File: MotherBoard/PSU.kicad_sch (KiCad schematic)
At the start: 51 parts, among them U401 LMR51430, U402 LMR51430

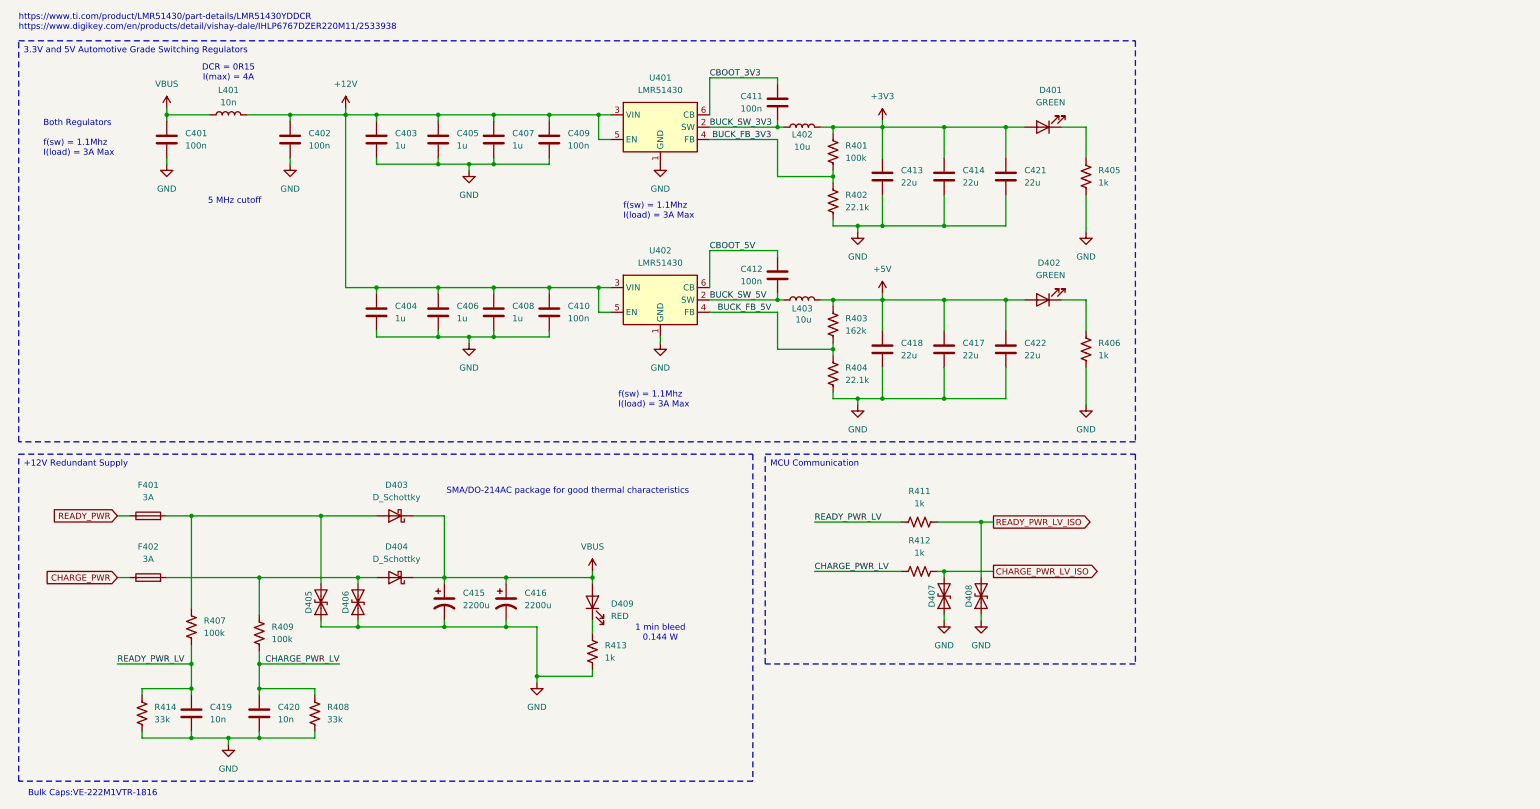
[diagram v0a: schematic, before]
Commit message: Redesigned EMI filters for switching regulators to meet CISPR 25 Class 5 EMI constraint + substituted BOM #s for JLC basic parts
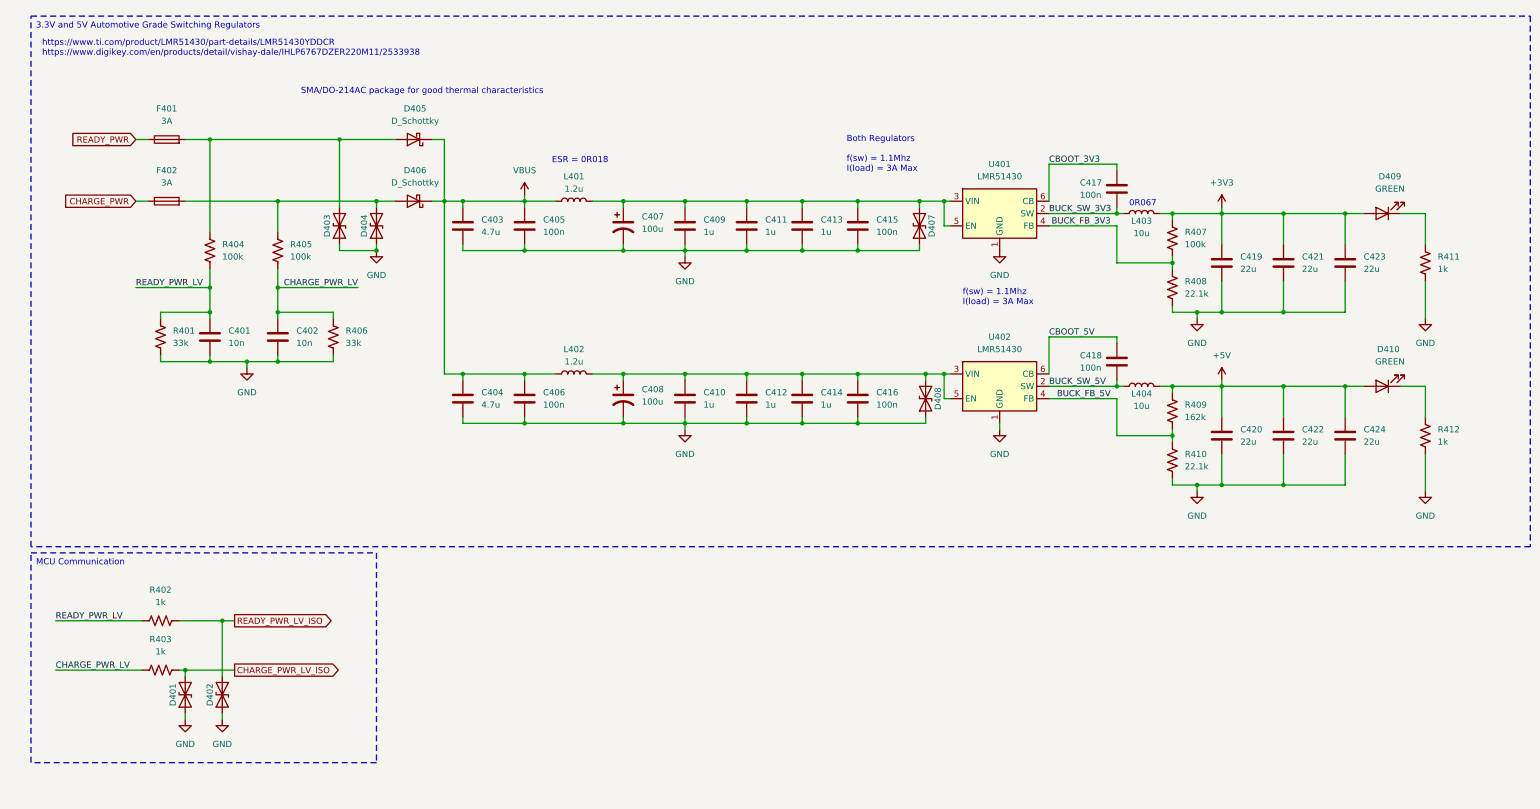
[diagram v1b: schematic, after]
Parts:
- removed C401, C402: 100n, Capacitor_SMD:C_0402_1005Metric, symbol Device:C
- removed C415, C416: 2200u, Capacitor_SMD:CP_Elec_18x17.5, symbol Device:C_Polarized_US
- removed D409: RED, LED_SMD:LED_0603_1608Metric, symbol Device:LED
- removed L403: 10u, symbol Device:L
- removed R413: 1k, Resistor_SMD:R_2512_6332Metric, symbol Device:R_US
- added C403, C404: 4.7u, Capacitor_SMD:C_1206_3216Metric, symbol Device:C
- added C405, C406: 100n, Capacitor_SMD:C_0402_1005Metric, symbol Device:C
- added C407, C408: 100u, Capacitor_SMD:CP_Elec_6.3x5.8, symbol Device:C_Polarized_US
- added D407, D408: D_TVS, Diode_SMD:D_SOD-323, symbol Device:D_TVS
- added L402: 1.2u, symbol Device:L
- added L404: 10u, Inductor_SMD:L_Sunlord_MWSA0603S, symbol Device:L
- C415: renamed from C409; footprint Capacitor_SMD:C_0603_1608Metric -> Capacitor_SMD:C_0402_1005Metric; Manufacturer_Part_Number CC0603KRX7R9BB104 -> CL05B104KO5NNNC
- C416: renamed from C410; footprint Capacitor_SMD:C_0603_1608Metric -> Capacitor_SMD:C_0402_1005Metric; Manufacturer_Part_Number CC0603KRX7R9BB104 -> CL05B104KO5NNNC
- L401: value 10n -> 1.2u
- L403: renamed from L402; footprint (none) -> Inductor_SMD:L_Sunlord_MWSA0603S; Manufacturer_Part_Number (none) -> MWSA0603S-100MT
- renumbered C419 to C401, C420 to C402, C403 to C409, C404 to C410, C405 to C411, C406 to C412, C407 to C413, C408 to C414, C411 to C417, C412 to C418, C413 to C419, C418 to C420, C414 to C421, C417 to C422, C421 to C423, C422 to C424, D407 to D401, D408 to D402, D405 to D403, D406 to D404, D403 to D405, D404 to D406, D401 to D409, D402 to D410, R414 to R401, R411 to R402, R412 to R403, R407 to R404, R409 to R405, R408 to R406, R401 to R407, R402 to R408, R403 to R409, R404 to R410, R405 to R411, R406 to R412
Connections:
- net +5V: now also L404.2
- net BUCK_SW_5V: now also L404.1
- net GND: now also C403.2, C404.2, C405.2, C406.2, C407.2, C408.2, D407.1 (A1), D408.1 (A1)
- net VBUS: now also C403.1, C404.1, C405.1, C406.1, L402.1
- net +12V: no longer names the net of C409.1, C411.1, C413.1, C415.1, L401.2, U401.3 (VIN), U401.5 (EN)
- net +12V: now also C407.1, D407.2 (A2); no longer C410.1, C412.1, C414.1, C416.1, U402.3 (VIN), U402.5 (EN)
- new net: C408.1, C410.1, C412.1, C414.1, C416.1, D408.2 (A2), L402.2, U402.3 (VIN), U402.5 (EN)
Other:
- note added: "0R067"
- note added: "ESR = 0R018"
- note removed: "1 min bleed 0.144 W"
- note removed: "5 MHz cutoff"
- note removed: "Bulk Caps:VE-222M1VTR-1816"
- note removed: "DCR = 0R15 I(max) = 4A"
- moved on the sheet: C401, C402, C409, C410, C411, C412, C413, C414, C415, C416, C417, C418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

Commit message: BOM completed + All 3D models added + Initial board shape complete
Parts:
- L401, L402: footprint (none) -> Inductor_SMD:L_Chilisin_BMRA00050530; Manufacturer_Part_Number (none) -> BMRA000505301R2MA1
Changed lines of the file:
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@@
 			)
 		)
-		(property "Footprint" ""
+		(property "Footprint" "Inductor_SMD:L_Chilisin_BMRA00050530"
 			(at 134.62 55.88 0)
 			(effects
@@
 			)
 		)
+		(property "Manufacturer_Part_Number" " BMRA000505301R2MA1"
+			(at 134.62 55.88 0)
+			(effects
+				(font
+					(size 1.27 1.27)
+				)
+				(hide yes)
+			)
+		)
 		(pin "2"
 		)
@@
 			)
 		)
-		(property "Footprint" ""
+		(property "Footprint" "Inductor_SMD:L_Chilisin_BMRA00050530"
 			(at 134.62 91.44 0)
 			(effects
@@
 			(at 134.62 91.44 0)
 			(effects
+				(font
+					(size 1.27 1.27)
+				)
+				(hide yes)
+			)
+		)
+		(property "Manufacturer_Part_Number" " BMRA000505301R2MA1"
+			(at 134.62 91.44 0)
+			(effects

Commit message: Finished layout need to route
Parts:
- removed D401, D402: D_TVS, Diode_SMD:D_SOD-323, symbol Device:D_TVS
- added D401, D402: D_Zener, symbol Device:D_Zener
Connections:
- net CHARGE_PWR_LV_ISO: now also D401.1 (K)
- net GND: now also D401.2 (A), D402.2 (A)
- net READY_PWR_LV_ISO: now also D402.1 (K)
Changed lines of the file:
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@@
 	)
 	(symbol
-		(lib_id "Device:D_TVS")
-		(at 54.61 157.48 90)
-		(unit 1)
-		(exclude_from_sim no)
-		(in_bom yes)
-		(on_board yes)
-		(dnp no)
-		(property "Reference" "D401"
-			(at 52.07 157.48 0)
-			(effects
-				(font
-					(size 1.27 1.27)
-				)
-			)
-		)
-		(property "Value" "D_TVS"
-			(at 57.15 157.48 0)
-			(effects
-				(font
-					(size 1.27 1.27)
-				)
-				(hide yes)
-			)
-		)
-		(property "Footprint" "Diode_SMD:D_SOD-323"
-			(at 54.61 157.48 0)
-			(effects
-				(font
-					(size 1.27 1.27)
-				)
-				(hide yes)
-			)
-		)
-		(property "Datasheet" "~"
-			(at 54.61 157.48 0)
-			(effects
-				(font
-					(size 1.27 1.27)
-				)
-				(hide yes)
-			)
-		)
-		(property "Description" "Bidirectional transient-voltage-suppression diode"
-			(at 54.61 157.48 0)
-			(effects
-				(font
-					(size 1.27 1.27)
-				)
-				(hide yes)
-			)
-		)
-		(property "Sim.Device" ""
-			(at 54.61 157.48 0)
-			(effects
-				(font
-					(size 1.27 1.27)
-				)
-				(hide yes)
-			)
-		)
-		(property "Sim.Pins" ""
-			(at 54.61 157.48 0)
-			(effects
-				(font
-					(size 1.27 1.27)
-				)
-				(hide yes)
-			)
-		)
-		(property "Sim.Type" ""
-			(at 54.61 157.48 0)
-			(effects
-				(font
-					(size 1.27 1.27)
-				)
-				(hide yes)
-			)
-		)
-		(pin "1"
-		)
-		(pin "2"
-		)
-		(instances
-			(project "FSAE_BMS"
-				(path "/335e81e9-b957-4266-8116-dde74329bfca/f9c85247-a583-4593-8eb2-5cacb3a96479"
-					(reference "D401")
-					(unit 1)
-				)
-			)
-		)
-	)
-	(symbol
 		(lib_id "Device:C_Polarized_US")
 		(at 144.78 60.96 0)
@@
 	)
 	(symbol
+		(lib_id "Device:D_Zener")
+		(at 54.61 157.48 270)
+		(unit 1)
+		(exclude_from_sim no)
+		(in_bom yes)
+		(on_board yes)
+		(dnp no)
+		(property "Reference" "D401"
+			(at 44.45 156.21 90)
+			(effects
+				(font
+					(size 1.27 1.27)
+				)
+				(justify left)
+			)
+		)
+		(property "Value" "D_Zener"
+			(at 44.45 158.75 90)
+			(effects
+				(font
+					(size 1.27 1.27)
+				)
+				(justify left)
+			)
+		)
+		(property "Footprint" ""
+			(at 54.61 157.48 0)
+			(effects
+				(font
+					(size 1.27 1.27)
+				)
+				(hide yes)
+			)
+		)
+		(property "Datasheet" "~"
+			(at 54.61 157.48 0)
+			(effects
+				(font
+					(size 1.27 1.27)
+				)
+				(hide yes)
+			)
+		)
+		(property "Description" "Zener diode"
+			(at 54.61 157.48 0)
+			(effects
+				(font
+					(size 1.27 1.27)
+				)
+				(hide yes)
+			)
+		)
+		(pin "1"
+		)
+		(pin "2"
+		)
+		(instances
+			(project ""
+				(path "/335e81e9-b957-4266-8116-dde74329bfca/f9c85247-a583-4593-8eb2-5cacb3a96479"
+					(reference "D401")
+					(unit 1)
+				)
+			)
+		)
+	)
+	(symbol
 		(lib_id "Device:C")
 		(at 246.38 53.34 0)
@@
 	)
 	(symbol
-		(lib_id "Device:D_TVS")
-		(at 62.23 157.48 90)
-		(unit 1)
-		(exclude_from_sim no)
-		(in_bom yes)
-		(on_board yes)
-		(dnp no)
-		(property "Reference" "D402"
-			(at 59.69 157.48 0)
-			(effects
-				(font
-					(size 1.27 1.27)
-				)
-			)
-		)
-		(property "Value" "D_TVS"
-			(at 64.77 157.48 0)
-			(effects
-				(font
-					(size 1.27 1.27)
-				)
-				(hide yes)
-			)
-		)
-		(property "Footprint" "Diode_SMD:D_SOD-323"
-			(at 62.23 157.48 0)
-			(effects
-				(font
-					(size 1.27 1.27)
-				)
-				(hide yes)
-			)
-		)
-		(property "Datasheet" "~"
-			(at 62.23 157.48 0)
-			(effects
-				(font
-					(size 1.27 1.27)
-				)
-				(hide yes)
-			)
-		)
-		(property "Description" "Bidirectional transient-voltage-suppression diode"
-			(at 62.23 157.48 0)
-			(effects
-				(font
-					(size 1.27 1.27)
-				)
-				(hide yes)
-			)
-		)
-		(property "Sim.Device" ""
-			(at 62.23 157.48 0)
-			(effects
-				(font
-					(size 1.27 1.27)
-				)
-				(hide yes)
-			)
-		)
-		(property "Sim.Pins" ""
-			(at 62.23 157.48 0)
-			(effects
-				(font
-					(size 1.27 1.27)
-				)
-				(hide yes)
-			)
-		)
-		(property "Sim.Type" ""
-			(at 62.23 157.48 0)
-			(effects
-				(font
-					(size 1.27 1.27)
-				)
-				(hide yes)
-			)
-		)
-		(pin "1"
-		)
-		(pin "2"
-		)
-		(instances
-			(project "FSAE_BMS"
-				(path "/335e81e9-b957-4266-8116-dde74329bfca/f9c85247-a583-4593-8eb2-5cacb3a96479"
-					(reference "D402")
-					(unit 1)
-				)
-			)
-		)
-	)
-	(symbol
 		(lib_id "Device:C")
 		(at 73.66 83.82 0)
@@
 	)
 	(symbol
+		(lib_id "Device:D_Zener")
+		(at 62.23 157.48 270)
+		(unit 1)
+		(exclude_from_sim no)
+		(in_bom yes)
+		(on_board yes)
+		(dnp no)
+		(fields_autoplaced yes)
+		(property "Reference" "D402"
+			(at 64.77 156.2099 90)
+			(effects
+				(font
+					(size 1.27 1.27)
+				)
+				(justify left)
+			)
+		)
+		(property "Value" "D_Zener"
+			(at 64.77 158.7499 90)
+			(effects
+				(font
+					(size 1.27 1.27)
+				)
+				(justify left)
+			)
+		)
+		(property "Footprint" ""
+			(at 62.23 157.48 0)
+			(effects
+				(font
+					(size 1.27 1.27)
+				)
+				(hide yes)
+			)
+		)
+		(property "Datasheet" "~"
+			(at 62.23 157.48 0)
+			(effects
+				(font
+					(size 1.27 1.27)
+				)
+				(hide yes)
+			)
+		)
+		(property "Description" "Zener diode"
+			(at 62.23 157.48 0)
+			(effects
+				(font
+					(size 1.27 1.27)
+				)
+				(hide yes)
+			)
+		)
+		(pin "1"
+		)
+		(pin "2"
+		)
+		(instances
+			(project "FSAE_BMS"
+				(path "/335e81e9-b957-4266-8116-dde74329bfca/f9c85247-a583-4593-8eb2-5cacb3a96479"
+					(reference "D402")
+					(unit 1)
+				)
+			)
+		)
+	)
+	(symbol
 		(lib_id "Device:C")
 		(at 59.69 83.82 0)
@@
 		(on_board yes)
 		(dnp no)
-		(fields_autoplaced yes)
 		(property "Reference" "C403"
 			(at 115.57 59.6899 0)

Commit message: Finished motherboard. Need to review BOM
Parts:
- removed R402, R403: 1k, Resistor_SMD:R_2512_6332Metric, symbol Device:R_US
- D401, D402: footprint (none) -> Diode_SMD:D_SOD-323; Manufacturer_Part_Number (none) -> LM3Z3V3T1G
- renumbered R404 to R402, R405 to R403, R406 to R404, R407 to R405, R408 to R406, R409 to R407, R410 to R408, R411 to R409, R412 to R410
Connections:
- net CHARGE_PWR_LV is gone; now on net CHARGE_PWR_LV_ISO: C402.1, R403.2, R404.1
- net READY_PWR_LV is gone; now on net READY_PWR_LV_ISO: C401.1, R401.1, R402.2
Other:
- moved on the sheet: D401

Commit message: Fixed power routing mistake + finished BOM + generated manufacturing files
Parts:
- D403, D404, D407, D408: footprint Diode_SMD:D_SOD-323 -> Diode_SMD:D_SOD-123; JLC (none) -> C353317; Manufacturer_Part_Number (none) -> SMF12CA

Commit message: Both boards complete
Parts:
- C401, C402: JLCPCB Part # (none) -> C60133
- C403, C404: JLCPCB Part # (none) -> C29823
- C405, C406, C415, C416, C417, C418: JLCPCB Part # (none) -> C1525
- C407, C408: JLCPCB Part # (none) -> C128464
- C409, C410, C411, C412, C413, C414: JLCPCB Part # (none) -> C28323
- C419, C420, C421, C422, C423, C424: JLCPCB Part # (none) -> C45783
- D401, D402: JLCPCB Part # (none) -> C46279
- D403, D404, D407, D408: JLC C353317 -> (none); JLCPCB Part # (none) -> C353317
- D405, D406: JLCPCB Part # (none) -> C22452
- D409, D410: JLCPCB Part # (none) -> C511604
- F401, F402: JLCPCB Part # (none) -> C182445
- L401, L402: JLCPCB Part # (none) -> C5296375
- L403, L404: JLCPCB Part # (none) -> C132141
- R401, R404: JLCPCB Part # (none) -> C25779
- R402, R403, R405: JLCPCB Part # (none) -> C25741
- R406, R408: JLCPCB Part # (none) -> C43473
- R407: JLCPCB Part # (none) -> C2998128
- R409, R410: JLCPCB Part # (none) -> C11702
- U401, U402: JLCPCB Part # (none) -> C5210749
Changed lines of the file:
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@@
 			)
 		)
-		(property "JLC" ""
+		(property "JLCPCB Part #" "C511604"
 			(at 300.99 93.98 0)
 			(effects
@@
 			)
 		)
-		(property "JLC" ""
+		(property "JLCPCB Part #" "C45783"
 			(at 267.97 68.58 0)
 			(effects
@@
 			)
 		)
-		(property "JLC" ""
+		(property "JLCPCB Part #" "C43473"
 			(at 257.81 109.22 0)
 			(effects
@@
 			)
 		)
-		(property "JLC" ""
+		(property "JLCPCB Part #" "C5296375"
 			(at 134.62 55.88 0)
 			(effects
@@
 			)
 		)
-		(property "JLC" " C353317"
+		(property "Manufacturer_Part_Number" "SMF12CA"
 			(at 205.74 60.96 0)
 			(effects
@@
 			)
 		)
-		(property "Manufacturer_Part_Number" "SMF12CA"
+		(property "JLCPCB Part #" "C353317"
 			(at 205.74 60.96 0)
 			(effects
@@
 			)
 		)
-		(property "JLC" ""
+		(property "JLCPCB Part #" "C128464"
 			(at 144.78 96.52 0)
 			(effects
@@
 			)
 		)
-		(property "JLC" ""
+		(property "JLCPCB Part #" "C25779"
 			(at 85.09 83.82 0)
 			(effects
@@
 			)
 		)
-		(property "JLC" ""
+		(property "JLCPCB Part #" "C128464"
 			(at 144.78 60.96 0)
 			(effects
@@
 			)
 		)
-		(property "JLC" ""
+		(property "JLCPCB Part #" "C28323"
 			(at 181.61 96.52 0)
 			(effects
@@
 			)
 		)
-		(property "JLC" " C353317"
+		(property "Manufacturer_Part_Number" "SMF12CA"
 			(at 207.01 96.52 0)
 			(effects
@@
 			)
 		)
-		(property "Manufacturer_Part_Number" "SMF12CA"
+		(property "JLCPCB Part #" "C353317"
 			(at 207.01 96.52 0)
 			(effects
@@
 			)
 		)
-		(property "JLC" ""
+		(property "JLCPCB Part #" "C46279"
 			(at 54.61 160.02 0)
 			(effects
@@
 			)
 		)
-		(property "JLC" ""
+		(property "JLCPCB Part #" "C1525"
 			(at 246.38 53.34 0)
 			(effects
@@
 			)
 		)
-		(property "JLC" ""
+		(property "JLCPCB Part #" "C28323"
 			(at 157.48 96.52 0)
 			(effects
@@
 			)
 		)
-		(property "JLC" ""
+		(property "JLCPCB Part #" "C11702"
 			(at 309.88 104.14 0)
 			(effects
@@
 			)
 		)
-		(property "JLC" ""
+		(property "JLCPCB Part #" "C1525"
 			(at 246.38 88.9 0)
 			(effects
@@
 			)
 		)
-		(property "JLC" ""
+		(property "JLCPCB Part #" "C45783"
 			(at 280.67 104.14 0)
 			(effects
@@
 			)
 		)
-		(property "JLC" ""
+		(property "JLCPCB Part #" "C1525"
 			(at 193.04 96.52 0)
 			(effects
@@
 			)
 		)
-		(property "JLC" ""
+		(property "JLCPCB Part #" "C1525"
 			(at 124.46 96.52 0)
 			(effects
@@
 			)
 		)
-		(property "JLC" ""
+		(property "JLCPCB Part #" "C45783"
 			(at 293.37 68.58 0)
 			(effects
@@
 			)
 		)
-		(property "JLC" ""
+		(property "JLCPCB Part #" "C28323"
 			(at 170.18 96.52 0)
 			(effects
@@
 			)
 		)
-		(property "JLC" " C353317"
+		(property "Manufacturer_Part_Number" "SMF12CA"
 			(at 93.98 60.96 0)
 			(effects
@@
 			)
 		)
-		(property "Manufacturer_Part_Number" "SMF12CA"
+		(property "JLCPCB Part #" "C353317"
 			(at 93.98 60.96 0)
 			(effects
@@
 			)
 		)
-		(property "JLC" ""
+		(property "JLCPCB Part #" "C1525"
 			(at 124.46 60.96 0)
 			(effects
@@
 			)
 		)
-		(property "JLC" ""
+		(property "JLCPCB Part #" "C60133"
 			(at 73.66 83.82 0)
 			(effects
@@
 			)
 		)
-		(property "JLC" ""
+		(property "JLCPCB Part #" "C25741"
 			(at 73.66 66.04 0)
 			(effects
@@
 			)
 		)
-		(property "JLC" ""
+		(property "JLCPCB Part #" "C22452"
 			(at 101.6 55.88 0)
 			(effects
@@
 			)
 		)
-		(property "JLC" ""
+		(property "JLCPCB Part #" "C28323"
 			(at 181.61 60.96 0)
 			(effects
@@
 			)
 		)
-		(property "JLC" ""
+		(property "JLCPCB Part #" "C132141"
 			(at 251.46 93.98 0)
 			(effects
@@
 			)
 		)
-		(property "JLC" ""
+		(property "JLCPCB Part #" "C28323"
 			(at 157.48 60.96 0)
 			(effects
@@
 			)
 		)
-		(property "JLC" ""
+		(property "JLCPCB Part #" "C45783"
 			(at 267.97 104.14 0)
 			(effects
@@
 			)
 		)
-		(property "JLC" ""
+		(property "JLCPCB Part #" "C25741"
 			(at 59.69 66.04 0)
 			(effects
@@
 			)
 		)
-		(property "JLC" ""
+		(property "JLCPCB Part #" "C1525"
 			(at 193.04 60.96 0)
 			(effects
@@
 			)
 		)
-		(property "JLC" ""
+		(property "JLCPCB Part #" "C22452"
 			(at 101.6 43.18 0)
 			(effects
@@
 			)
 		)
-		(property "JLC" ""
+		(property "JLCPCB Part #" "C46279"
 			(at 62.23 160.02 0)
 			(effects
@@
 			)
 		)
-		(property "JLC" " C353317"
+		(property "Manufacturer_Part_Number" "SMF12CA"
 			(at 86.36 60.96 0)
 			(effects
@@
 			)
 		)
-		(property "Manufacturer_Part_Number" "SMF12CA"
+		(property "JLCPCB Part #" "C353317"
 			(at 86.36 60.96 0)
 			(effects
@@
 			)
 		)
-		(property "JLC" ""
+		(property "JLCPCB Part #" "C2998128"
 			(at 257.81 99.06 0)
 			(effects
@@
 			)
 		)
-		(property "JLC" ""
+		(property "JLCPCB Part #" "C5296375"
 			(at 134.62 91.44 0)
 			(effects
@@
 			)
 		)
-		(property "JLC" ""
+		(property "JLCPCB Part #" "C25779"
 			(at 49.53 83.82 0)
 			(effects
@@
 			)
 		)
-		(property "JLC" ""
+		(property "JLCPCB Part #" "C60133"
 			(at 59.69 83.82 0)
 			(effects
@@
 			)
 		)
-		(property "JLC" ""
+		(property "JLCPCB Part #" "C28323"
 			(at 170.18 60.96 0)
 			(effects
@@
 			)
 		)
-		(property "JLC" ""
+		(property "JLCPCB Part #" "C5210749"
 			(at 222.25 93.98 0)
 			(effects
@@
 			)
 		)
-		(property "JLC" ""
+		(property "JLCPCB Part #" "C511604"
 			(at 300.99 58.42 0)
 			(effects
@@
 			)
 		)
-		(property "JLC" ""
+		(property "JLCPCB Part #" "C5210749"
 			(at 222.25 58.42 0)
 			(effects
@@
 			)
 		)
-		(property "JLC" ""
+		(property "JLCPCB Part #" "C182445"
 			(at 50.8 55.88 0)
 			(effects
@@
 			)
 		)
-		(property "JLC" ""
+		(property "JLCPCB Part #" "C182445"
 			(at 50.8 43.18 0)
 			(effects
@@
 			)
 		)
-		(property "JLC" ""
+		(property "JLCPCB Part #" "C29823"
 			(at 111.76 96.52 0)
 			(effects
@@
 			)
 		)
-		(property "JLC" ""
+		(property "JLCPCB Part #" "C45783"
 			(at 293.37 104.14 0)
 			(effects
@@
 			)
 		)
-		(property "JLC" ""
+		(property "JLCPCB Part #" "C43473"
 			(at 257.81 73.66 0)
 			(effects
@@
 			)
 		)
-		(property "JLC" ""
+		(property "JLCPCB Part #" "C25741"
 			(at 257.81 63.5 0)
 			(effects
@@
 			)
 		)
-		(property "JLC" ""
+		(property "JLCPCB Part #" "C132141"
 			(at 251.46 58.42 0)
 			(effects
@@
 			)
 		)
-		(property "JLC" ""
+		(property "JLCPCB Part #" "C45783"
 			(at 280.67 68.58 0)
 			(effects
@@
 			)
 		)
-		(property "JLC" ""
+		(property "JLCPCB Part #" "C11702"
 			(at 309.88 68.58 0)
 			(effects
@@
 			)
 		)
-		(property "JLC" ""
+		(property "JLCPCB Part #" "C29823"
 			(at 111.76 60.96 0)
 			(effects
